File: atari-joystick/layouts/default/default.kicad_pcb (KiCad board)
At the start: 2 copper layers, 31.5 x 35 mm, 9 parts

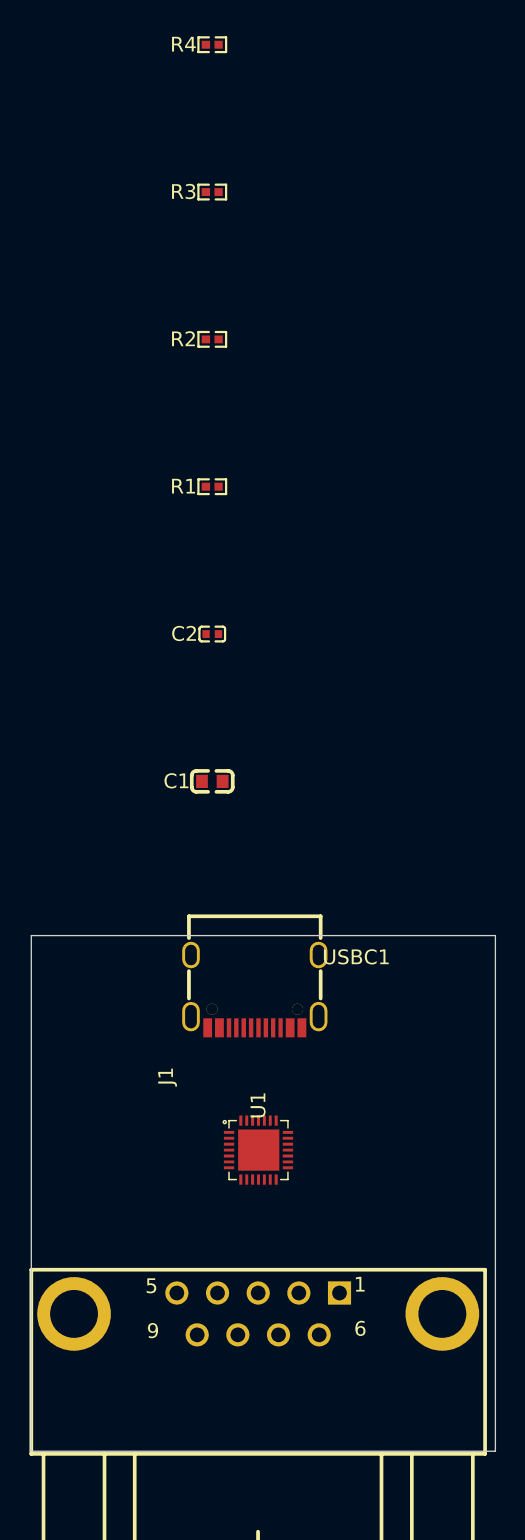
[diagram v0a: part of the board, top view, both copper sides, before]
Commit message: atari-joystick: デバッグ LED 追加と 3D モデルオフセット永続化
- parts/leds.ato: 緑/赤 0603 LED の wrapper module (LedGreen0603 /
  LedRed0603) を追加。anode/cathode の signal 名を統一。
- parts/Everlight_..._3T (LCSC C72043, 緑) と
  parts/Hubei_KENTO_..._KT-0603R (LCSC C2286, 赤) を ato create part で取得
- atari_joystick.ato: 抽象 LED → 上記 wrapper に差し替え。BOM/PCB から
  silent drop していた問題を解消 (LED1, LED2 が PCB に乗るように)
- 3D モデルオフセットを .kicad_mod に転記して永続化:
  - DSUB:  offset (-1.27 0 0), rotate (0 0 -90)
  - USB-C: offset (0 -2.54 0)
  - QFN28: offset (0 0 0.74)
- README.md: 共通 MCU の表記を F8U6/TSSOP-20 → G8U6/QFN-28 に修正

Co-Authored-By: Claude Opus 4.7 (1M context) <noreply@anthropic.com>
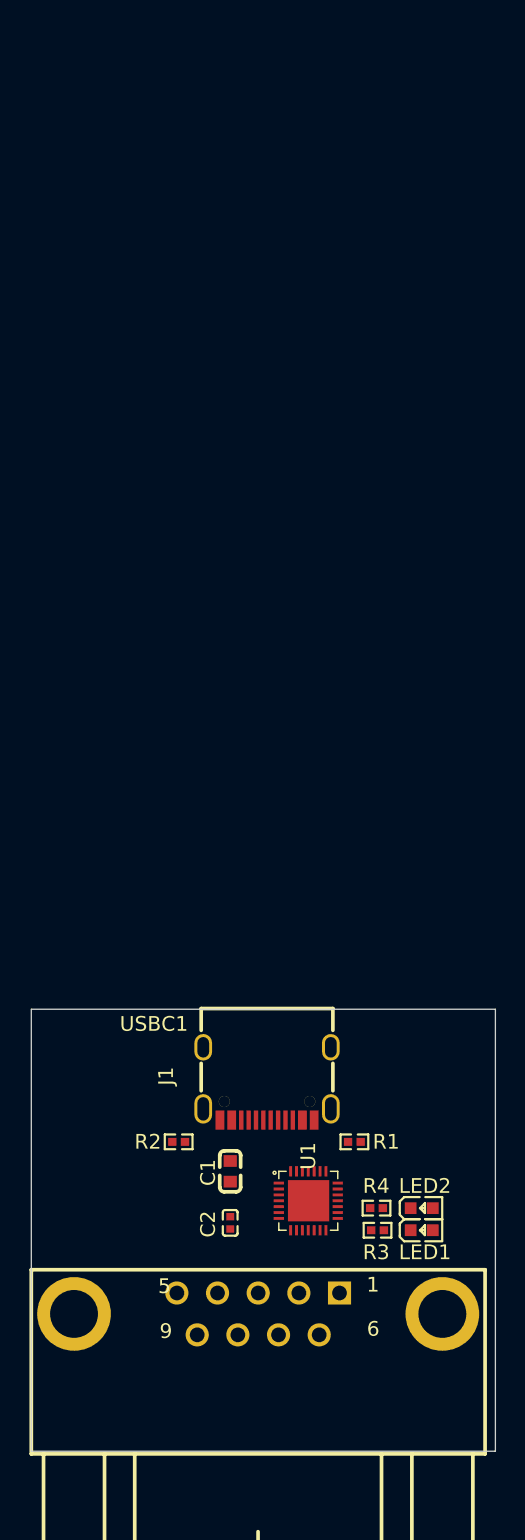
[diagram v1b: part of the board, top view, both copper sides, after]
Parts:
- added LED1: , Everlight_Elec_19_217_GHC_YR1S2_3T:LED0603-RD, F.Cu at (126.5, 135.0)
- added LED2: , Hubei_KENTO_Elec_KT_0603R:LED0603-RD, F.Cu at (126.5, 133.5)
- moved R4 79.8 mm to (123.4, 133.5), turned to 180 degrees
- moved R3 71.4 mm to (123.5, 135.0), turned to 180 degrees
- moved R2 54.5 mm to (110.0, 129.0), turned to 180 degrees
- moved R1 45.5 mm to (121.9, 129.0)
- moved C2 40.0 mm to (113.5, 134.5), turned to -90 degrees
- moved C1 26.5 mm to (113.5, 131.0), turned to -90 degrees
- moved USBC1 6.32 mm to (116.0, 125.1)
- moved U1 4.82 mm to (118.8, 133.0)
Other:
- board size 31.5 x 35 mm -> 31.5 x 30 mm

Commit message: atari-joystick: VBUS と MCU の間に 3.3V LDO を挿入し USB 互換性を確保
CH32X035 の USB FS トランシーバの D+/D- 出力レベルは VDD に直結している
ため、VDD = 5V (VBUS 直結) のままだと D+ アイドル電圧が 5V となり USB 規格
(VOH max ≈ 3.6V) を逸脱する。iPhone / Mac は寛容で問題なく動作するが、
Pixel 等の規格準拠ホスト (Android) では enumerate されない。

主な変更:
- LP5907MFX-3.3 (LCSC C23380874) ベースの Ldo3V3 モジュールを新設
  (parts/ldo_3v3.ato) し、入出力に 1µF デカップリングを実装
- atari_joystick.ato で vdd33 レールを新設し、VBUS → LDO → VDD33 → MCU
  の経路に変更。LED アノードと BOOT ボタンソースも VDD33 へ移動して
  D+ への 5V 印加を防止
- 3.3V 駆動に合わせて LED 直列抵抗を 1kΩ → 470Ω に調整
- docs/CH32X035.md に「USB 通信時の VDD 必須事項」節を追加し、デバッグ時の
  D+ 電圧テスタ確認手順を記載
- 各 .ato ファイルのコメント・docstring を日本語化

Co-Authored-By: Claude Opus 4.7 (1M context) <noreply@anthropic.com>
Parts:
- added C3: 1µF ±10%, Samsung_Electro_Mechanics_CL05A105KA5NQNC:C0402, F.Cu at (106.5, 134.4)
- added C4: 1µF ±10%, Samsung_Electro_Mechanics_CL05A105KA5NQNC:C0402, F.Cu at (102.5, 136.5)
- added R5: 4.7kΩ ±1%, UNI_ROYAL_0402WGF4701TCE:R0402, F.Cu at (122.5, 121.0)
- added SW1: , XKB_Connectivity_TS_1187A_B_A_B:SW-SMD_4P-L5.1-W5.1-P3.70-LS6.5-TL_H1.5, F.Cu at (126.0, 124.0)
- added U2: , TECH_PUBLIC_LP5907MFX_3_3:SOT-23-5_L3.0-W1.7-P0.95-LS2.8-BR, F.Cu at (103.3, 133.9)
- R3, R4: value 1kΩ ±1% -> 470Ω ±1%; footprint UNI_ROYAL_0402WGF1001TCE:R0402 -> UNI_ROYAL_0402WGF4700TCE:R0402
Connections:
- C1 pad 1: VBUS -> VDD33
- C2 pad 1: VBUS -> VDD33
- LED1 pad 2: VBUS -> VDD33
- LED2 pad 2: VBUS -> VDD33
- U1 pad 2: VBUS -> VDD33

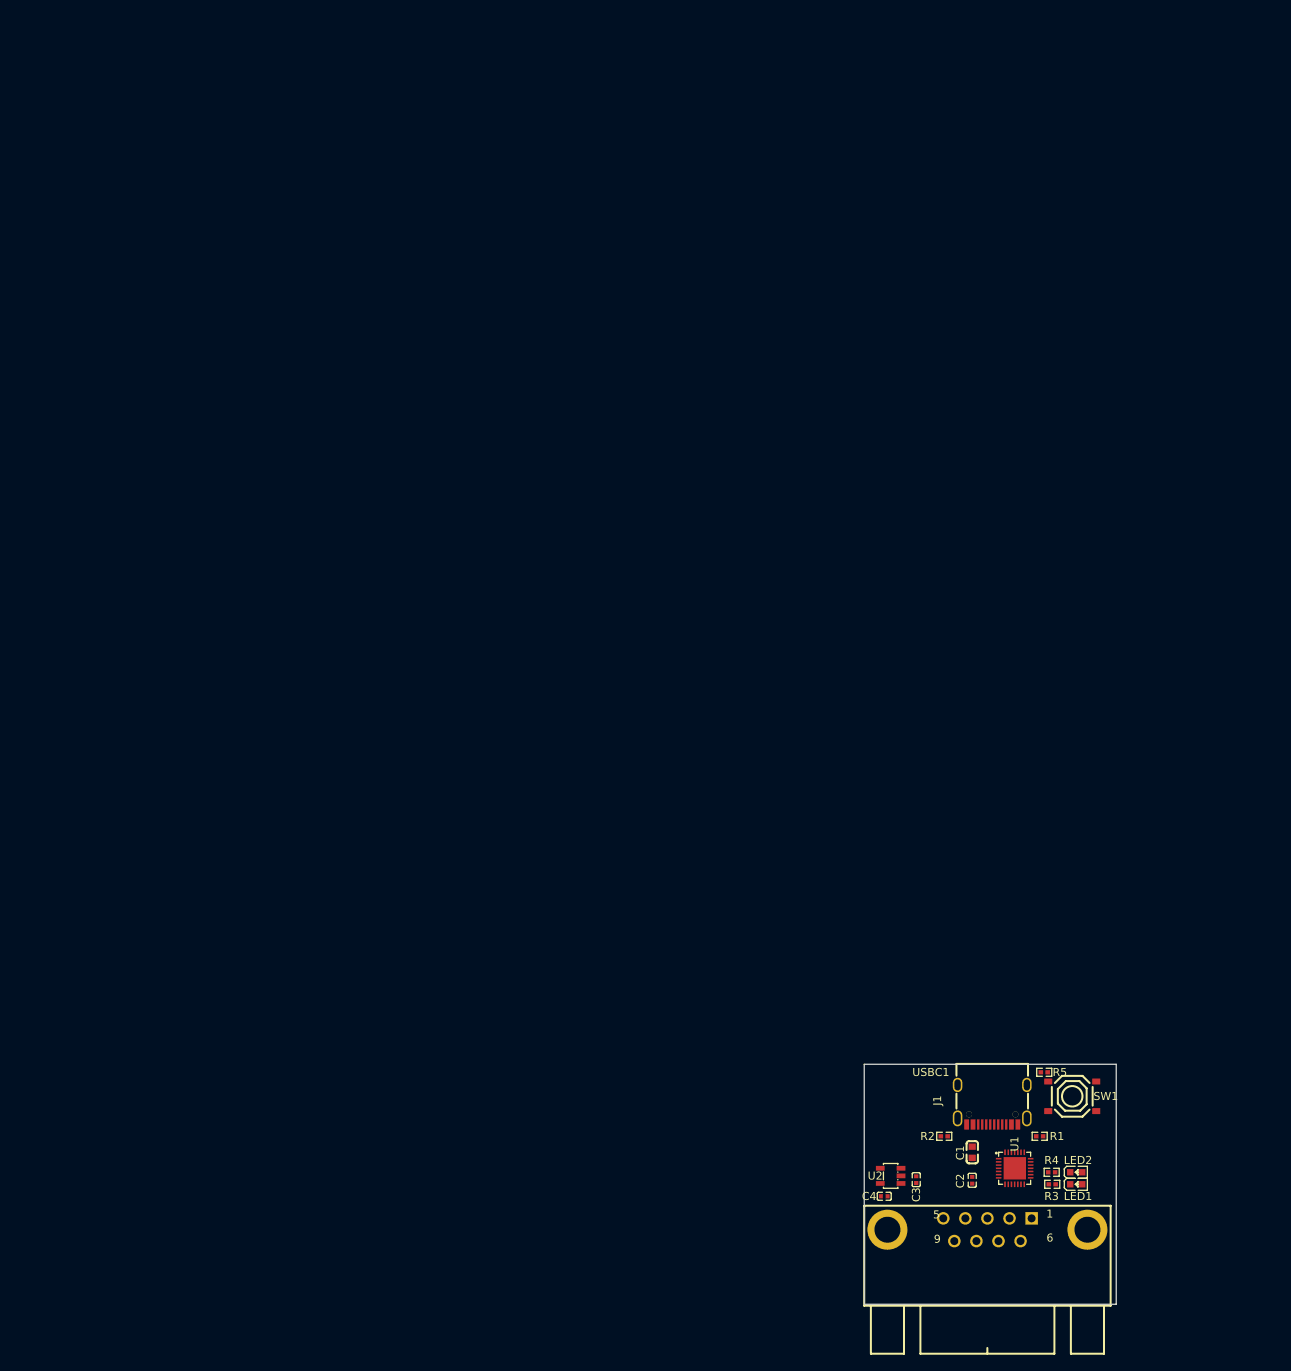
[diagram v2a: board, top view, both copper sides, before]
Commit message: x68000-keyboard 基板の初版実装と両基板へのレベルシフタ統合
- x68000-keyboard を新規追加: CH32X035G8U6 + USB-C + LDO + TC7MPB9307FT
  経由で Mini DIN 7pin から X68000 キーボード/マウス信号を駆動
- atari-joystick にも TC7MPB9307FT を追加 (CH32X035 は 5V トレラントでなく、
  X68000 側 5V 信号と直結すると絶対最大定格を超え破損するため)
- TC7MPB9307FT は ato create part で自動生成版を取得し level_shifter.ato
  を nOE 引数仕様に追従
- x68000-keyboard の BOOT ボタンは XUNPU TS-1088 (2 ピン、3.9×3.0mm) を採用
- Mini DIN 7pin は手配コネクタ前提のため KiCad フットプリントはダミー
  プレースホルダ (`MiniDIN-7P_PLACEHOLDER`) を仮割当

Co-Authored-By: Claude Opus 4.7 (1M context) <noreply@anthropic.com>
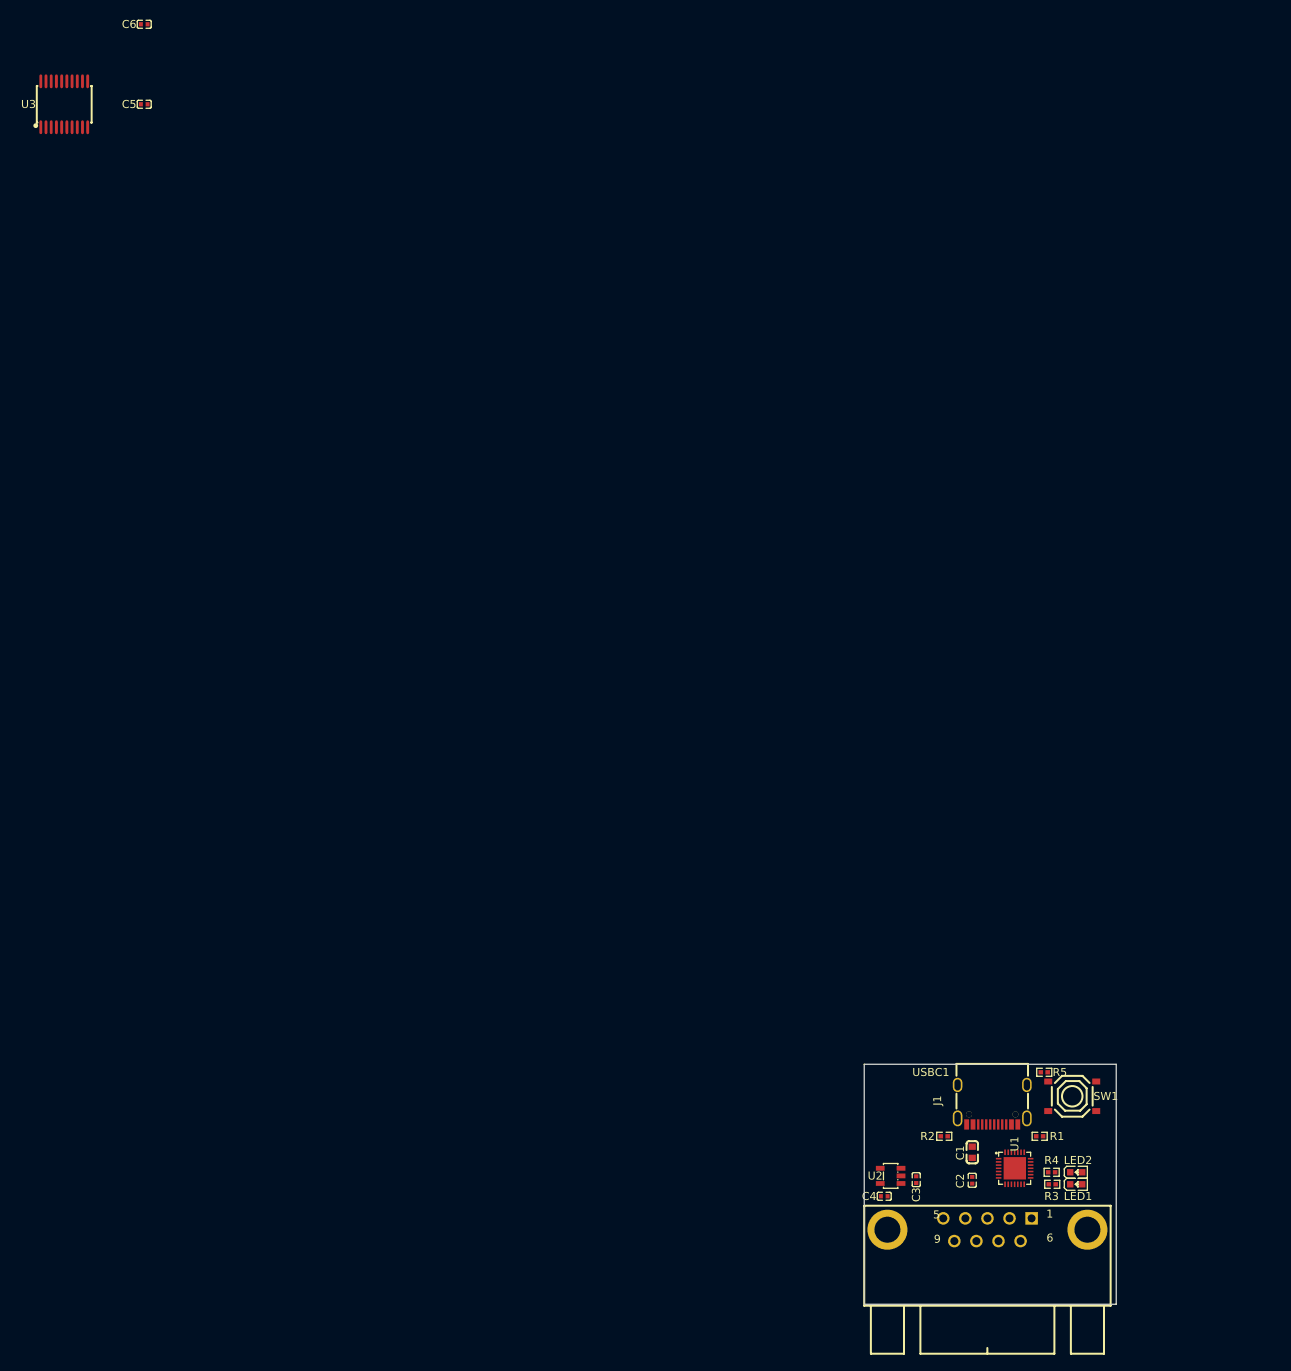
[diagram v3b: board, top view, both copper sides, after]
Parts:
- added C5: 100nF ±10%, Samsung_Electro_Mechanics_CL05B104KO5NNNC:C0402, F.Cu at (10.0, 0.00)
- added C6: 100nF ±10%, Samsung_Electro_Mechanics_CL05B104KO5NNNC:C0402, F.Cu at (10.0, -10.0)
- added U3: , TOSHIBA_TC7MPB9307FT_EL:TSSOP-20_L6.5-W4.4-P0.65-LS6.5-BL, F.Cu at (0.00, 0.00)
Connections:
- R3 pad 2: PB3 -> PB11
- R4 pad 2: PB4 -> PB12_T1C4_T2C2N_
- U1 pad 11: triga -> PA6
- U1 pad 12: up -> PA7
- U1 pad 5: common -> PA0
- U1 pad 6: right -> PA1
- U1 pad 7: left -> PA2
- U1 pad 8: trigb -> PA3
- U1 pad 9: down -> PA4

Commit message: 両基板: USB-C CC1/CC2 を MCU PC14/PC15 に接続して USB-PD 検出を有効化
CH32X035 の内蔵 USB-PD コントローラが CC ラインを直接サンプリングできるよう、
従来は 5.1kΩ プルダウンで終端していた CC1/CC2 を MCU の専用ピン PC14 (CC1) /
PC15 (CC2) にも分岐させる。プルダウン経由で 5V 系の Rp 分圧 (max ~1.7V @ 3A
広告) しか印加されないため MCU の絶対最大定格 (VDD+0.3V = 3.6V) は満たされる。

Co-Authored-By: Claude Opus 4.7 (1M context) <noreply@anthropic.com>
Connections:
- R1 pad 1: cc1 -> PC14_CC1_T1C3_T2C2_
- R2 pad 1: cc2 -> PC15_CC2_T2C3_T1ET_
- USBC1 pad A5: cc1 -> PC14_CC1_T1C3_T2C2_
- USBC1 pad B5: cc2 -> PC15_CC2_T2C3_T1ET_
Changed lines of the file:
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@@
 		)
 	)
-	(net 1 "PC15_CC2_T2C3_T1ET_")
 	(net 3 "PB0")
 	(net 4 "PB3")
@@
 	(net 13 "PC19")
 	(net 14 "PC18_DIO_TX3_T2C1N_T3C2_I2C_T1ET_")
-	(net 15 "PC14_CC1_T1C3_T2C2_")
 	(net 16 "PC0")
 	(net 17 "PC3")
 	(net 18 "PB4")
 	(net 19 "usbc-shell")
-	(net 20 "cc1")
 	(net 21 "sbu1")
-	(net 22 "cc2")
 	(net 23 "dn")
 	(net 24 "sbu2")
@@
 	(net 58 "PA3")
 	(net 59 "PA4")
+	(net 2 "PC14_CC1_T1C3_T2C2_")
+	(net 11 "PC15_CC2_T2C3_T1ET_")
 	(footprint "Everlight_Elec_19_217_GHC_YR1S2_3T:LED0603-RD"
 		(layer "F.Cu")
@@
 			(size 0.57 0.54)
 			(layers "F.Cu" "F.Paste" "F.Mask")
-			(net 20 "cc1")
+			(net 2 "PC14_CC1_T1C3_T2C2_")
 		)
 		(pad "2" smd rect
@@
 			(size 0.3 1.3)
 			(layers "F.Cu" "F.Paste" "F.Mask")
-			(net 20 "cc1")
+			(net 2 "PC14_CC1_T1C3_T2C2_")
 		)
 		(pad "A6" smd rect
@@
 			(size 0.3 1.3)
 			(layers "F.Cu" "F.Paste" "F.Mask")
-			(net 22 "cc2")
+			(net 11 "PC15_CC2_T2C3_T1ET_")
 		)
 		(pad "B6" smd rect
@@
 			(size 0.2 0.7)
 			(layers "F.Cu" "F.Paste" "F.Mask")
-			(net 1 "PC15_CC2_T2C3_T1ET_")
+			(net 11 "PC15_CC2_T2C3_T1ET_")
 		)
 		(pad "2" smd rect
@@
 			(size 0.7 0.2)
 			(layers "F.Cu" "F.Paste" "F.Mask")
-			(net 15 "PC14_CC1_T1C3_T2C2_")
+			(net 2 "PC14_CC1_T1C3_T2C2_")
 		)
 		(pad "29" smd rect
@@
 			(size 0.57 0.54)
 			(layers "F.Cu" "F.Paste" "F.Mask")
-			(net 22 "cc2")
+			(net 11 "PC15_CC2_T2C3_T1ET_")
 		)
 		(pad "2" smd rect

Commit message: 両基板: MCU〜レベルシフタ間の信号ネットに用途名を付与
物理ピン名 (PB8, PA3 など) のままでは .ato ソースも生成回路図/ネットリスト
も読みづらいため、MCU 側〜レベルシフタ A 側に中間 signal を挿し、
has_net_name トレイトで用途名 (KEY_TXD_3V3, UP_3V3 など) を割り当てる。
KiCad 上のネット名表示も意味のある名前になる。

Co-Authored-By: Claude Opus 4.7 (1M context) <noreply@anthropic.com>
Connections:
- net PA0 renamed COMMON_3V3
- net PA2 renamed RIGHT_3V3
- net PA3 renamed LEFT_3V3
- net PA4 renamed TRIGB_3V3
- net PA5 renamed DOWN_3V3
- net PA6 renamed TRIGA_3V3
- net PA7 renamed UP_3V3
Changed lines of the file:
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@@
 	(net 49 "left")
 	(net 50 "down")
-	(net 51 "PA2")
-	(net 52 "PA6")
-	(net 53 "PA0")
-	(net 54 "PA5")
-	(net 55 "PA7")
+	(net 51 "RIGHT_3V3")
+	(net 52 "TRIGA_3V3")
+	(net 53 "COMMON_3V3")
+	(net 54 "DOWN_3V3")
+	(net 55 "UP_3V3")
 	(net 56 "PB11")
 	(net 57 "PB12_T1C4_T2C2N_")
-	(net 58 "PA3")
-	(net 59 "PA4")
+	(net 58 "LEFT_3V3")
+	(net 59 "TRIGB_3V3")
 	(net 2 "PC14_CC1_T1C3_T2C2_")
 	(net 11 "PC15_CC2_T2C3_T1ET_")
@@
 			(size 0.2 0.7)
 			(layers "F.Cu" "F.Paste" "F.Mask")
-			(net 53 "PA0")
+			(net 53 "COMMON_3V3")
 		)
 		(pad "6" smd rect
@@
 			(size 0.2 0.7)
 			(layers "F.Cu" "F.Paste" "F.Mask")
-			(net 51 "PA2")
+			(net 51 "RIGHT_3V3")
 		)
 		(pad "8" smd rect
@@
 			(size 0.7 0.2)
 			(layers "F.Cu" "F.Paste" "F.Mask")
-			(net 58 "PA3")
+			(net 58 "LEFT_3V3")
 		)
 		(pad "9" smd rect
@@
 			(size 0.7 0.2)
 			(layers "F.Cu" "F.Paste" "F.Mask")
-			(net 59 "PA4")
+			(net 59 "TRIGB_3V3")
 		)
 		(pad "10" smd rect
@@
 			(size 0.7 0.2)
 			(layers "F.Cu" "F.Paste" "F.Mask")
-			(net 54 "PA5")
+			(net 54 "DOWN_3V3")
 		)
 		(pad "11" smd rect
@@
 			(size 0.7 0.2)
 			(layers "F.Cu" "F.Paste" "F.Mask")
-			(net 52 "PA6")
+			(net 52 "TRIGA_3V3")
 		)
 		(pad "12" smd rect
@@
 			(size 0.7 0.2)
 			(layers "F.Cu" "F.Paste" "F.Mask")
-			(net 55 "PA7")
+			(net 55 "UP_3V3")
 		)
 		(pad "13" smd rect
@@
 			(size 0.36 1.74)
 			(layers "F.Cu" "F.Paste" "F.Mask")
-			(net 55 "PA7")
+			(net 55 "UP_3V3")
 		)
 		(pad "3" smd oval
@@
 			(size 0.36 1.74)
 			(layers "F.Cu" "F.Paste" "F.Mask")
-			(net 54 "PA5")
+			(net 54 "DOWN_3V3")
 		)
 		(pad "4" smd oval
@@
 			(size 0.36 1.74)
 			(layers "F.Cu" "F.Paste" "F.Mask")
-			(net 58 "PA3")
+			(net 58 "LEFT_3V3")
 		)
 		(pad "5" smd oval
@@
 			(size 0.36 1.74)
 			(layers "F.Cu" "F.Paste" "F.Mask")
-			(net 51 "PA2")
+			(net 51 "RIGHT_3V3")
 		)
 		(pad "6" smd oval
@@
 			(size 0.36 1.74)
 			(layers "F.Cu" "F.Paste" "F.Mask")
-			(net 52 "PA6")
+			(net 52 "TRIGA_3V3")
 		)
 		(pad "7" smd oval
@@
 			(size 0.36 1.74)
 			(layers "F.Cu" "F.Paste" "F.Mask")
-			(net 59 "PA4")
+			(net 59 "TRIGB_3V3")
 		)
 		(pad "8" smd oval
@@
 			(size 0.36 1.74)
 			(layers "F.Cu" "F.Paste" "F.Mask")
-			(net 53 "PA0")
+			(net 53 "COMMON_3V3")
 		)
 		(pad "9" smd oval

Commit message: atari-joystick: レベルシフタ B 側電源を VBUS から VCC_HOST に変更
x68000-keyboard と同じ流儀で、レベルシフタの 5V 側 (VCCB) を USB VBUS では
なく D-SUB Pin 5 から供給されるホスト側 +5V に切り替える。X68000 / Mega
Drive はどちらも Pin 5 で +5V を供給するため通常用途で問題なく、VBUS と
ホスト電源の逆流リスクを回避できる。新たに `vcc_host` 電源レール (ネット
名 "VCC_HOST") を追加し、`joy.vcc` を接続。README も 3 レール構成
(VBUS / VDD33 / VCC_HOST) に書き直し。

Co-Authored-By: Claude Opus 4.7 (1M context) <noreply@anthropic.com>
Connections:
- C6 pad 1: VBUS -> VCC_HOST
- J1 pad 5: vcc -> VCC_HOST
- U3 pad 20: VBUS -> VCC_HOST
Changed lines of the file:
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@@
 	(net 25 "shell")
 	(net 26 "PA1")
-	(net 27 "vcc")
 	(net 34 "cathode-1")
 	(net 35 "cathode")
@@
 	(net 2 "PC14_CC1_T1C3_T2C2_")
 	(net 11 "PC15_CC2_T2C3_T1ET_")
+	(net 1 "VCC_HOST")
 	(footprint "Everlight_Elec_19_217_GHC_YR1S2_3T:LED0603-RD"
 		(layer "F.Cu")
@@
 			(drill 0.999998)
 			(layers "*.Cu" "*.Mask")
-			(net 27 "vcc")
+			(net 1 "VCC_HOST")
 		)
 		(pad "6" thru_hole circle
@@
 			(size 0.36 1.74)
 			(layers "F.Cu" "F.Paste" "F.Mask")
-			(net 45 "VBUS")
+			(net 1 "VCC_HOST")
 		)
 		(pad "19" smd oval
@@
 			(size 0.5 0.54)
 			(layers "F.Cu" "F.Paste" "F.Mask")
-			(net 45 "VBUS")
+			(net 1 "VCC_HOST")
 		)
 		(embedded_fonts no)
